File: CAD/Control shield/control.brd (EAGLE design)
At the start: 49.5 x 19.3 mm, 8 parts

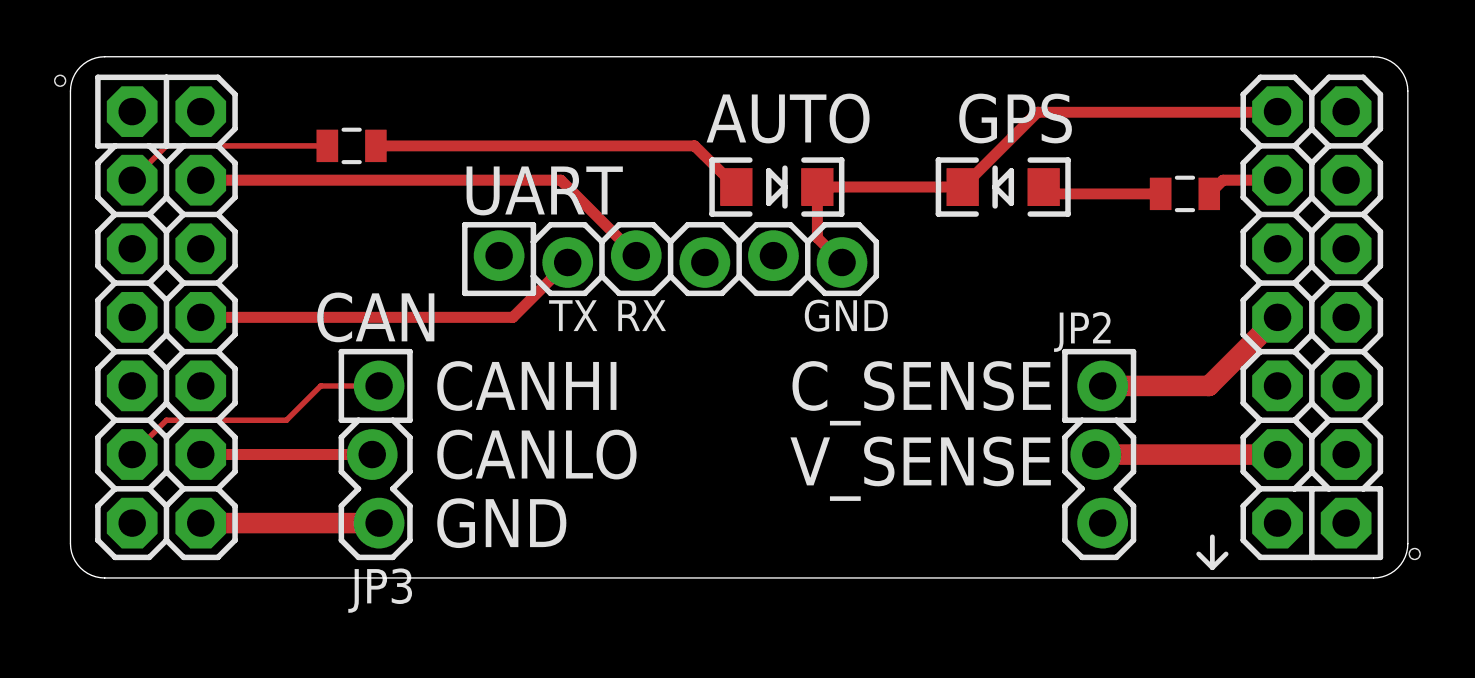
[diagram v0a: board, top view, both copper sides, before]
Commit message: Updated all CANode shields to fit the latest version of it.
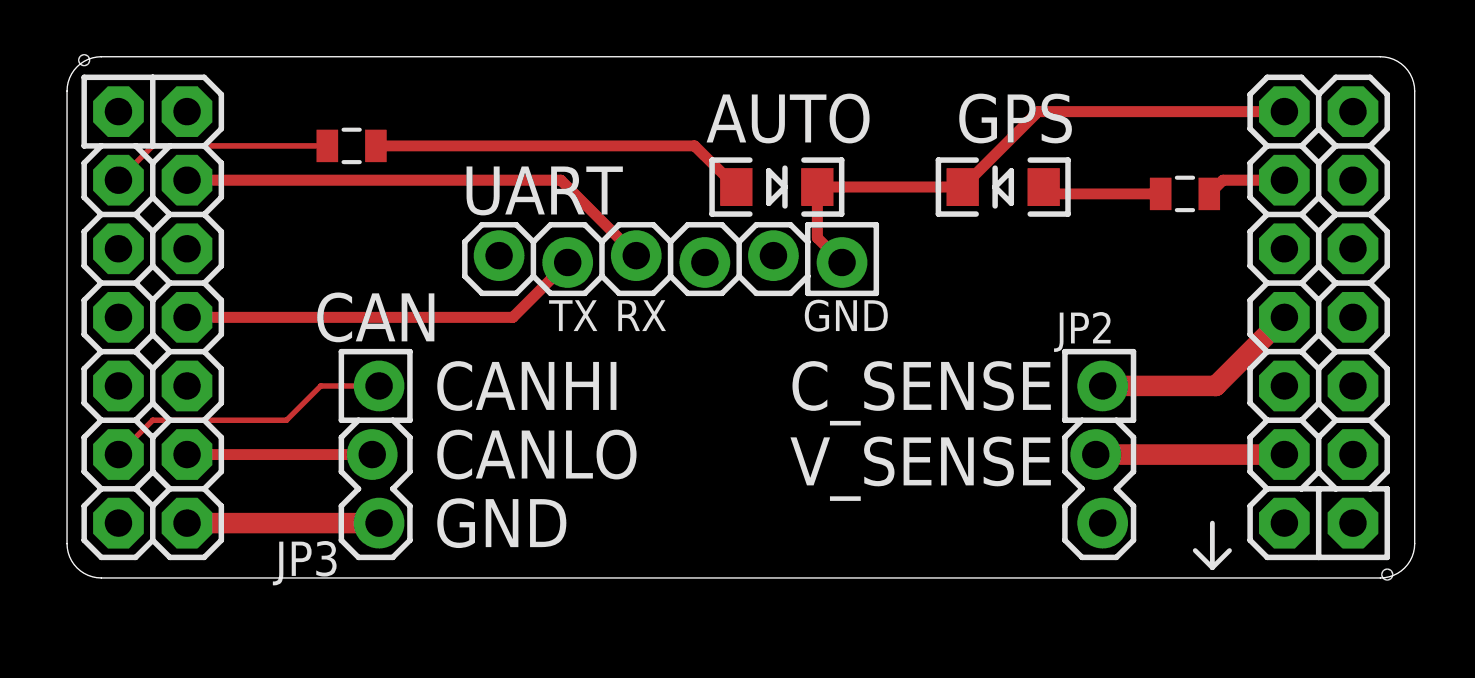
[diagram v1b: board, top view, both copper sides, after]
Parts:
- moved JP1 12.7 mm to (28.7, 18.7), turned to 180 degrees
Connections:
- net GND2: now also JP1.1; no longer JP1.6
- net UART_RX: now also JP1.4; no longer JP1.3
- net UART_TX: now also JP1.5; no longer JP1.2
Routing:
- net LED_AUTOMODE: track 7.75 -> 8.26 mm
- net GND4: track 6.60 -> 7.11 mm
- net CAN_LO: track 6.35 -> 6.86 mm
- net UART_TX: track 14.4 -> 14.9 mm
- net UART_RX: track 17.3 -> 17.8 mm
- net CAN_HI: track 10.2 -> 10.7 mm
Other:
- board size 49.5 x 19.3 mm -> 49.9 x 19.3 mm
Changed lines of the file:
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@@
 <text x="22.225" y="17.145" size="1.143" layer="21" font="vector" ratio="14" rot="R180">RX</text>
 <text x="30.48" y="17.145" size="1.143" layer="21" font="vector" ratio="14" rot="R180">GND</text>
-<wire x1="0.127" y1="24.892" x2="0.127" y2="8.128" width="0" layer="20"/>
-<wire x1="0.127" y1="8.128" x2="1.397" y2="6.858" width="0" layer="20" curve="90"/>
-<wire x1="1.397" y1="6.858" x2="48.387" y2="6.858" width="0" layer="20"/>
-<wire x1="48.387" y1="6.858" x2="49.657" y2="8.128" width="0" layer="20" curve="90"/>
-<wire x1="49.657" y1="8.128" x2="49.657" y2="24.892" width="0" layer="20"/>
-<wire x1="49.657" y1="24.892" x2="48.387" y2="26.162" width="0" layer="20" curve="90"/>
-<wire x1="48.387" y1="26.162" x2="1.397" y2="26.162" width="0" layer="20"/>
-<wire x1="1.397" y1="26.162" x2="0.127" y2="24.892" width="0" layer="20" curve="90"/>
-<wire x1="42.418" y1="7.239" x2="42.418" y2="8.382" width="0.1778" layer="21"/>
-<wire x1="42.418" y1="7.239" x2="42.926" y2="7.747" width="0.1778" layer="21"/>
-<wire x1="42.418" y1="7.239" x2="41.91" y2="7.747" width="0.1778" layer="21"/>
+<wire x1="0" y1="24.892" x2="0" y2="8.128" width="0" layer="20"/>
+<wire x1="0" y1="8.128" x2="1.27" y2="6.858" width="0" layer="20" curve="90"/>
+<wire x1="1.27" y1="6.858" x2="48.641" y2="6.858" width="0" layer="20"/>
+<wire x1="48.641" y1="6.858" x2="49.911" y2="8.128" width="0" layer="20" curve="90"/>
+<wire x1="49.911" y1="8.128" x2="49.911" y2="24.892" width="0" layer="20"/>
+<wire x1="49.911" y1="24.892" x2="48.641" y2="26.162" width="0" layer="20" curve="90"/>
+<wire x1="48.641" y1="26.162" x2="1.27" y2="26.162" width="0" layer="20"/>
+<wire x1="1.27" y1="26.162" x2="0" y2="24.892" width="0" layer="20" curve="90"/>
+<wire x1="42.418" y1="7.239" x2="42.418" y2="8.89" width="0.1778" layer="21"/>
+<wire x1="42.418" y1="7.239" x2="43.053" y2="7.874" width="0.1778" layer="21"/>
+<wire x1="42.418" y1="7.239" x2="41.783" y2="7.874" width="0.1778" layer="21"/>
 </plain>
 <attributes>
@@
 </element>
 <element name="JP3" library="ASL" package="1X03_LOCK" value="M03LOCK" x="11.43" y="13.97" smashed="yes" rot="R270">
-<attribute name="NAME" x="12.9032" y="7.1882" size="1.27" layer="25" ratio="15" rot="R180"/>
+<attribute name="NAME" x="10.1092" y="8.2042" size="1.27" layer="25" ratio="15" rot="R180"/>
 </element>
-<element name="JP1" library="ASL" package="1X06_LOCK" value="" x="16.002" y="18.669" smashed="yes"/>
+<element name="JP1" library="ASL" package="1X06_LOCK" value="" x="28.702" y="18.669" smashed="yes" rot="R180"/>
 </elements>
 <signals>
@@
 <contactref element="U$1" pad="RB1"/>
 <contactref element="JP2" pad="1"/>
-<wire x1="38.354" y1="13.97" x2="42.291" y2="13.97" width="0.762" layer="1"/>
-<wire x1="42.291" y1="13.97" x2="44.831" y2="16.51" width="0.762" layer="1"/>
+<wire x1="38.354" y1="13.97" x2="42.545" y2="13.97" width="0.762" layer="1"/>
+<wire x1="42.545" y1="13.97" x2="45.085" y2="16.51" width="0.762" layer="1"/>
 </signal>
 <signal name="VOLTAGE_SENSE">
 <contactref element="U$1" pad="A0"/>
 <contactref element="JP2" pad="2"/>
-<wire x1="44.831" y1="11.43" x2="38.1" y2="11.43" width="0.762" layer="1"/>
+<wire x1="45.085" y1="11.43" x2="38.1" y2="11.43" width="0.762" layer="1"/>
 </signal>
 <signal name="LED_AUTOMODE" class="2">
 <contactref element="U$1" pad="RB12"/>
 <contactref element="R2" pad="2"/>
-<wire x1="2.413" y1="21.59" x2="3.683" y2="22.86" width="0.2032" layer="1"/>
-<wire x1="3.683" y1="22.86" x2="9.641" y2="22.86" width="0.2032" layer="1"/>
+<wire x1="1.905" y1="21.59" x2="3.175" y2="22.86" width="0.2032" layer="1"/>
+<wire x1="3.175" y1="22.86" x2="9.641" y2="22.86" width="0.2032" layer="1"/>
 </signal>
 <signal name="LED_GPS">
 <contactref element="U$1" pad="RB15"/>
 <contactref element="R1" pad="2"/>
-<wire x1="44.831" y1="21.59" x2="42.81" y2="21.59" width="0.4064" layer="1"/>
+<wire x1="45.085" y1="21.59" x2="42.81" y2="21.59" width="0.4064" layer="1"/>
 <wire x1="42.81" y1="21.59" x2="42.302" y2="21.082" width="0.4064" layer="1"/>
 </signal>
@@
 <contactref element="LED2" pad="C"/>
 <contactref element="U$1" pad="GND"/>
-<wire x1="44.807" y1="24.106" x2="44.831" y2="24.13" width="0.4064" layer="1"/>
-<wire x1="44.807" y1="24.106" x2="35.941" y2="24.106" width="0.4064" layer="1"/>
-<wire x1="35.941" y1="24.106" x2="33.171" y2="21.336" width="0.4064" layer="1"/>
+<wire x1="35.965" y1="24.13" x2="33.171" y2="21.336" width="0.4064" layer="1"/>
 <wire x1="27.789" y1="21.336" x2="33.171" y2="21.336" width="0.4064" layer="1"/>
-<contactref element="JP1" pad="6"/>
-<wire x1="27.789" y1="21.336" x2="27.789" y2="19.455" width="0.4064" layer="1"/>
-<wire x1="27.789" y1="19.455" x2="28.702" y2="18.542" width="0.4064" layer="1"/>
+<wire x1="45.085" y1="24.13" x2="35.965" y2="24.13" width="0.4064" layer="1"/>
+<contactref element="JP1" pad="1"/>
+<wire x1="28.702" y1="18.542" x2="27.789" y2="19.455" width="0.4064" layer="1"/>
+<wire x1="27.789" y1="19.455" x2="27.789" y2="21.336" width="0.4064" layer="1"/>
 </signal>
 <signal name="GND3">
@@
 <contactref element="JP3" pad="2"/>
 <contactref element="U$1" pad="CAN_LOW"/>
-<wire x1="4.953" y1="11.43" x2="11.303" y2="11.43" width="0.4064" layer="1"/>
+<wire x1="4.445" y1="11.43" x2="11.303" y2="11.43" width="0.4064" layer="1"/>
 </signal>
 <signal name="CAN_HI" class="2">
 <contactref element="JP3" pad="1"/>
 <contactref element="U$1" pad="CAN_HIGH"/>
-<wire x1="2.413" y1="11.43" x2="3.683" y2="12.7" width="0.2032" layer="1"/>
-<wire x1="3.683" y1="12.7" x2="8.128" y2="12.7" width="0.2032" layer="1"/>
+<wire x1="1.905" y1="11.43" x2="3.175" y2="12.7" width="0.2032" layer="1"/>
+<wire x1="3.175" y1="12.7" x2="8.128" y2="12.7" width="0.2032" layer="1"/>
 <wire x1="8.128" y1="12.7" x2="9.398" y2="13.97" width="0.2032" layer="1"/>
 <wire x1="9.398" y1="13.97" x2="11.557" y2="13.97" width="0.2032" layer="1"/>
@@
 <contactref element="U$1" pad="GND4"/>
 <contactref element="JP3" pad="3"/>
-<wire x1="11.557" y1="8.89" x2="4.953" y2="8.89" width="0.762" layer="1"/>
+<wire x1="11.557" y1="8.89" x2="4.445" y2="8.89" width="0.762" layer="1"/>
 </signal>
 <signal name="UART_RX">
-<contactref element="JP1" pad="3"/>
 <contactref element="U$1" pad="RB9"/>
-<wire x1="21.082" y1="18.796" x2="18.288" y2="21.59" width="0.4064" layer="1"/>
-<wire x1="18.288" y1="21.59" x2="4.953" y2="21.59" width="0.4064" layer="1"/>
+<wire x1="18.288" y1="21.59" x2="4.445" y2="21.59" width="0.4064" layer="1"/>
+<contactref element="JP1" pad="4"/>
+<wire x1="18.288" y1="21.59" x2="21.082" y2="18.796" width="0.4064" layer="1"/>
 </signal>
 <signal name="UART_TX">
-<contactref element="JP1" pad="2"/>
 <contactref element="U$1" pad="RB8"/>
-<wire x1="4.953" y1="16.51" x2="16.51" y2="16.51" width="0.4064" layer="1"/>
+<wire x1="4.445" y1="16.51" x2="16.51" y2="16.51" width="0.4064" layer="1"/>
+<contactref element="JP1" pad="5"/>
 <wire x1="16.51" y1="16.51" x2="18.542" y2="18.542" width="0.4064" layer="1"/>
 </signal>
